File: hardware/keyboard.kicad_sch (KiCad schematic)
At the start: 48 parts, among them SW1 SW_Push, SW10 SW_Push, SW11 SW_Push, SW12 SW_Push, SW13 SW_Push, SW14 SW_Push, SW15 SW_Push, SW16 SW_Push, SW17 SW_Push, SW18 SW_Push, SW19 SW_Push, SW2 SW_Push, SW20 SW_Push, SW21 SW_Push, SW22 SW_Push, SW23 SW_Push, SW25 SW_Push, SW26 SW_Push, SW27 SW_Push, SW28 SW_Push, SW29 SW_Push, SW3 SW_Push, SW30 SW_Push, SW31 SW_Push, SW33 SW_Push, SW34 SW_Push, SW35 SW_Push, SW36 SW_Push, SW37 SW_Push, SW38 SW_Push, SW39 SW_Push, SW4 SW_Push, SW5 SW_Push, SW58 SKRHABE010, SW6 SW_Push, SW7 SW_Push, SW9 SW_Push, U11 PCA9555PW

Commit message: Cleanup project library
Add hexpansion connector symbol, footprint and 3d
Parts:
- SW1, SW10, SW11, SW12, SW13, SW14, SW15, SW16, SW17, SW18, SW19, SW2, SW20, SW21, SW22, SW23, SW25, SW26, SW27, SW28, SW29, SW3, SW30, SW31, SW33, SW34, SW35, SW36, SW37, SW38, SW39, SW4, SW5, SW6, SW7, SW9: footprint lib:bottonepiccolo_C2888430 -> badge:bottonepiccolo_C2888430
- SW58: footprint lib:SKRHABE010_ALPS -> badge:SKRHABE010_ALPS; symbol 2024-05-18_00-01-46:SKRHABE010 -> badge:SKRHABE010
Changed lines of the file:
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@@
 			)
 		)
-		(property "Footprint" "lib:bottonepiccolo_C2888430"
+		(property "Footprint" "badge:bottonepiccolo_C2888430"
 			(at 153.67 121.92 0)
 			(effects
@@
 			)
 		)
-		(property "Footprint" "lib:bottonepiccolo_C2888430"
+		(property "Footprint" "badge:bottonepiccolo_C2888430"
 			(at 132.08 109.22 0)
 			(effects
@@
 			)
 		)
-		(property "Footprint" "lib:bottonepiccolo_C2888430"
+		(property "Footprint" "badge:bottonepiccolo_C2888430"
 			(at 172.72 83.82 0)
 			(effects
@@
 			)
 		)
-		(property "Footprint" "lib:bottonepiccolo_C2888430"
+		(property "Footprint" "badge:bottonepiccolo_C2888430"
 			(at 132.08 71.12 0)
 			(effects
@@
 			)
 		)
-		(property "Footprint" "lib:bottonepiccolo_C2888430"
+		(property "Footprint" "badge:bottonepiccolo_C2888430"
 			(at 110.49 71.12 0)
 			(effects
@@
 			)
 		)
-		(property "Footprint" "lib:bottonepiccolo_C2888430"
+		(property "Footprint" "badge:bottonepiccolo_C2888430"
 			(at 132.08 121.92 0)
 			(effects
@@
 			)
 		)
-		(property "Footprint" "lib:bottonepiccolo_C2888430"
+		(property "Footprint" "badge:bottonepiccolo_C2888430"
 			(at 132.08 58.42 0)
 			(effects
@@
 			)
 		)
-		(property "Footprint" "lib:bottonepiccolo_C2888430"
+		(property "Footprint" "badge:bottonepiccolo_C2888430"
 			(at 172.72 58.42 0)
 			(effects
@@
 			)
 		)
-		(property "Footprint" "lib:bottonepiccolo_C2888430"
+		(property "Footprint" "badge:bottonepiccolo_C2888430"
 			(at 153.67 109.22 0)
 			(effects
@@
 			)
 		)
-		(property "Footprint" "lib:bottonepiccolo_C2888430"
+		(property "Footprint" "badge:bottonepiccolo_C2888430"
 			(at 110.49 83.82 0)
 			(effects
@@
 			)
 		)
-		(property "Footprint" "lib:bottonepiccolo_C2888430"
+		(property "Footprint" "badge:bottonepiccolo_C2888430"
 			(at 172.72 71.12 0)
 			(effects
@@
 	)
 	(symbol
-		(lib_id "2024-05-18_00-01-46:SKRHABE010")
+		(lib_id "badge:SKRHABE010")
 		(at 160.02 163.83 0)
 		(mirror y)
@@
 			)
 		)
-		(property "Footprint" "lib:SKRHABE010_ALPS"
+		(property "Footprint" "badge:SKRHABE010_ALPS"
 			(at 160.02 163.83 0)
 			(effects
@@
 			)
 		)
-		(property "Footprint" "lib:bottonepiccolo_C2888430"
+		(property "Footprint" "badge:bottonepiccolo_C2888430"
 			(at 191.77 83.82 0)
 			(effects
@@
 			)
 		)
-		(property "Footprint" "lib:bottonepiccolo_C2888430"
+		(property "Footprint" "badge:bottonepiccolo_C2888430"
 			(at 153.67 83.82 0)
 			(effects
@@
 			)
 		)
-		(property "Footprint" "lib:bottonepiccolo_C2888430"
+		(property "Footprint" "badge:bottonepiccolo_C2888430"
 			(at 191.77 109.22 0)
 			(effects
@@
 			)
 		)
-		(property "Footprint" "lib:bottonepiccolo_C2888430"
+		(property "Footprint" "badge:bottonepiccolo_C2888430"
 			(at 110.49 96.52 0)
 			(effects
@@
 			)
 		)
-		(property "Footprint" "lib:bottonepiccolo_C2888430"
+		(property "Footprint" "badge:bottonepiccolo_C2888430"
 			(at 172.72 121.92 0)
 			(effects
@@
 			)
 		)
-		(property "Footprint" "lib:bottonepiccolo_C2888430"
+		(property "Footprint" "badge:bottonepiccolo_C2888430"
 			(at 172.72 96.52 0)
 			(effects
@@
 			)
 		)
-		(property "Footprint" "lib:bottonepiccolo_C2888430"
+		(property "Footprint" "badge:bottonepiccolo_C2888430"
 			(at 191.77 58.42 0)
 			(effects
@@
 			)
 		)
-		(property "Footprint" "lib:bottonepiccolo_C2888430"
+		(property "Footprint" "badge:bottonepiccolo_C2888430"
 			(at 132.08 96.52 0)
 			(effects
@@
 			)
 		)
-		(property "Footprint" "lib:bottonepiccolo_C2888430"
+		(property "Footprint" "badge:bottonepiccolo_C2888430"
 			(at 153.67 58.42 0)
 			(effects
@@
 			)
 		)
-		(property "Footprint" "lib:bottonepiccolo_C2888430"
+		(property "Footprint" "badge:bottonepiccolo_C2888430"
 			(at 153.67 134.62 0)
 			(effects
@@
 			)
 		)
-		(property "Footprint" "lib:bottonepiccolo_C2888430"
+		(property "Footprint" "badge:bottonepiccolo_C2888430"
 			(at 210.82 134.62 0)
 			(effects
@@
 			)
 		)
-		(property "Footprint" "lib:bottonepiccolo_C2888430"
+		(property "Footprint" "badge:bottonepiccolo_C2888430"
 			(at 110.49 109.22 0)
 			(effects
@@
 			)
 		)
-		(property "Footprint" "lib:bottonepiccolo_C2888430"
+		(property "Footprint" "badge:bottonepiccolo_C2888430"
 			(at 110.49 134.62 0)
 			(effects
@@
 			)
 		)
-		(property "Footprint" "lib:bottonepiccolo_C2888430"
+		(property "Footprint" "badge:bottonepiccolo_C2888430"
 			(at 110.49 121.92 0)
 			(effects
@@
 			)
 		)
-		(property "Footprint" "lib:bottonepiccolo_C2888430"
+		(property "Footprint" "badge:bottonepiccolo_C2888430"
 			(at 153.67 96.52 0)
 			(effects
@@
 			)
 		)
-		(property "Footprint" "lib:bottonepiccolo_C2888430"
+		(property "Footprint" "badge:bottonepiccolo_C2888430"
 			(at 191.77 71.12 0)
 			(effects
@@
 			)
 		)
-		(property "Footprint" "lib:bottonepiccolo_C2888430"
+		(property "Footprint" "badge:bottonepiccolo_C2888430"
 			(at 172.72 109.22 0)
 			(effects
@@
 			)
 		)
-		(property "Footprint" "lib:bottonepiccolo_C2888430"
+		(property "Footprint" "badge:bottonepiccolo_C2888430"
 			(at 172.72 134.62 0)
 			(effects
@@
 			)
 		)
-		(property "Footprint" "lib:bottonepiccolo_C2888430"
+		(property "Footprint" "badge:bottonepiccolo_C2888430"
 			(at 153.67 71.12 0)
 			(effects
@@
 			)
 		)
-		(property "Footprint" "lib:bottonepiccolo_C2888430"
+		(property "Footprint" "badge:bottonepiccolo_C2888430"
 			(at 132.08 134.62 0)
 			(effects
@@
 			)
 		)
-		(property "Footprint" "lib:bottonepiccolo_C2888430"
+		(property "Footprint" "badge:bottonepiccolo_C2888430"
 			(at 191.77 96.52 0)
 			(effects
@@
 			)
 		)
-		(property "Footprint" "lib:bottonepiccolo_C2888430"
+		(property "Footprint" "badge:bottonepiccolo_C2888430"
 			(at 191.77 134.62 0)
 			(effects
@@
 			)
 		)
-		(property "Footprint" "lib:bottonepiccolo_C2888430"
+		(property "Footprint" "badge:bottonepiccolo_C2888430"
 			(at 132.08 83.82 0)
 			(effects
@@
 			)
 		)
-		(property "Footprint" "lib:bottonepiccolo_C2888430"
+		(property "Footprint" "badge:bottonepiccolo_C2888430"
 			(at 191.77 121.92 0)
 			(effects
@@
 			)
 		)
-		(property "Footprint" "lib:bottonepiccolo_C2888430"
+		(property "Footprint" "badge:bottonepiccolo_C2888430"
 			(at 110.49 58.42 0)
 			(effects

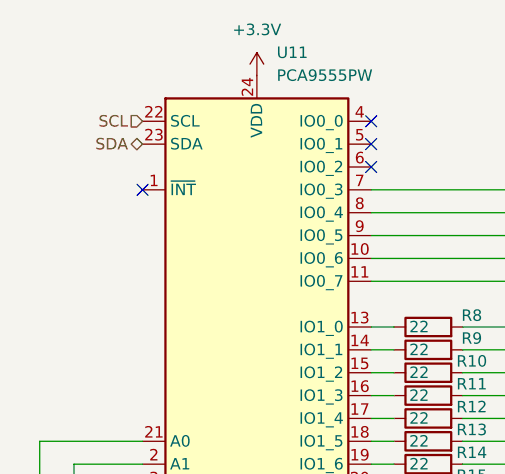
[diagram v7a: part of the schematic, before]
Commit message: Add sdcard fooprint
Remove io expander
Reorganize a bit the mcu schematic
Routed audio
Routed lora
Partial pin swapping of esp32 for facilitating routing
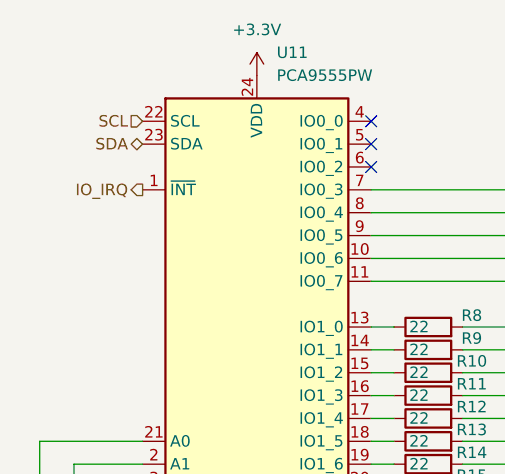
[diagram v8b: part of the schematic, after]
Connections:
- net IO_IRQ: now reaches U11.1 (~{INT})
- no-connect marks 4 -> 3
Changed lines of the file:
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@@
 		(at 63.5 43.18)
-	)
-	(no_connect
-		(at 38.1 48.26)
 	)
 	(wire
@@
 		(fields_autoplaced yes)
 		(effects
+			(font
+				(size 1.27 1.27)
+			)
+			(justify right)
+		)
+	)
+	(hierarchical_label "IO_IRQ"
+		(shape output)
+		(at 38.1 48.26 180)
+		(fields_autoplaced yes)
+		(effects
